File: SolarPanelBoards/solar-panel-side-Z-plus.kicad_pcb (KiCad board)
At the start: 2 copper layers, 97 x 97.4 mm, 23 parts, among them J1 Conn_01x06, J3 Conn_01x02, U1 OPT3001DNPT

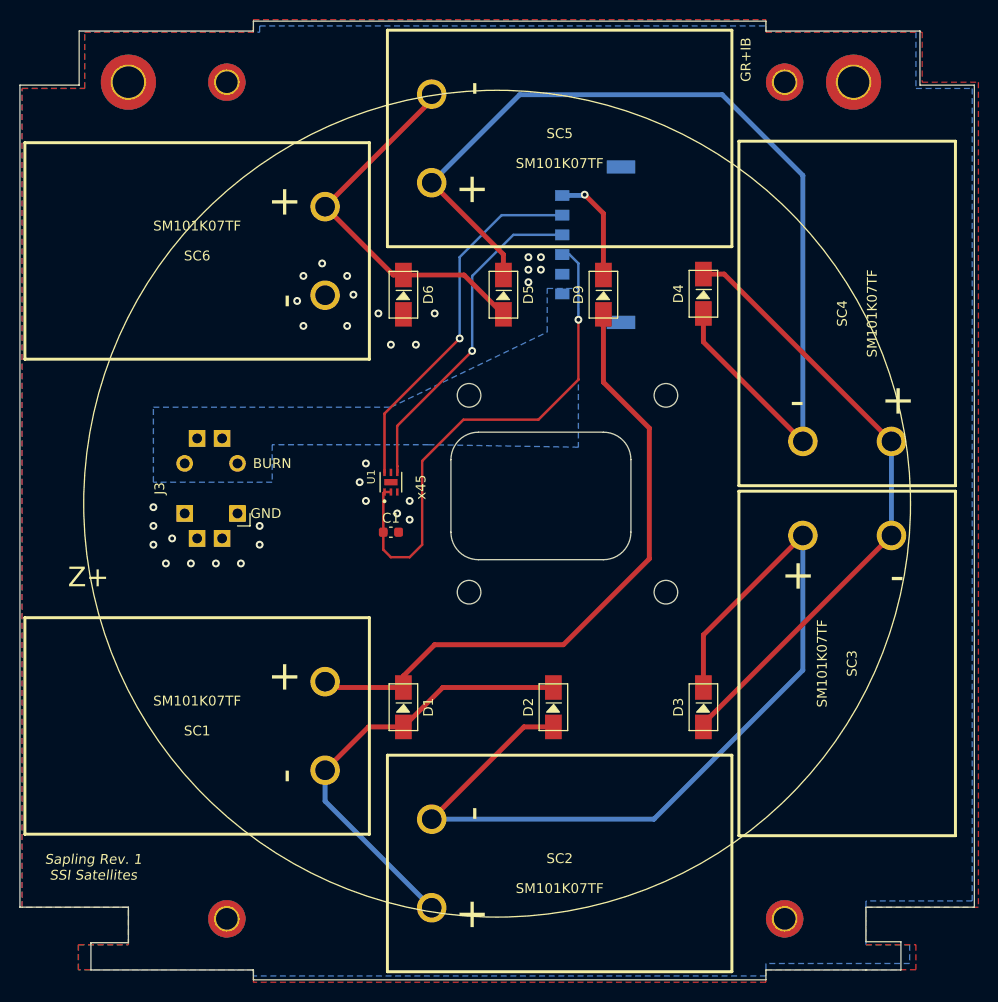
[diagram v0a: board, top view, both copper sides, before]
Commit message: Battery board and side panels ready for CAD check and review, pycubed not finished yet
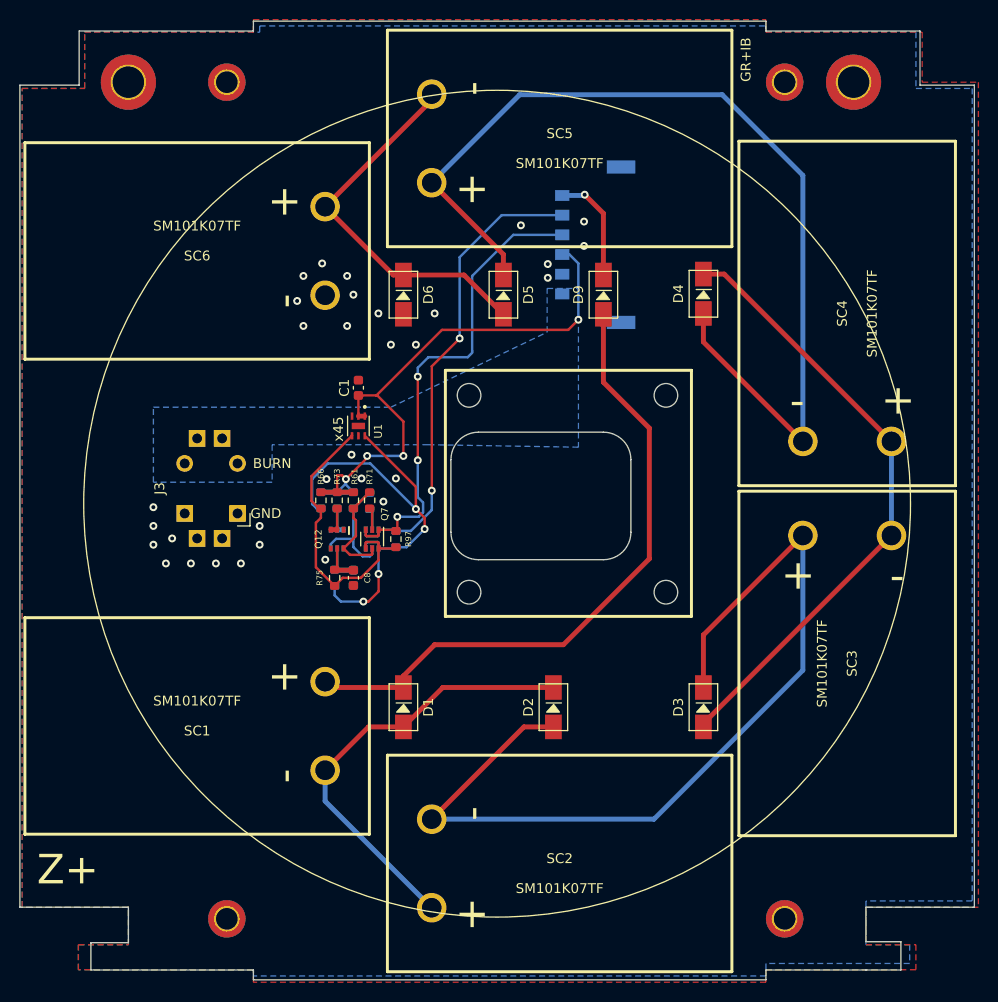
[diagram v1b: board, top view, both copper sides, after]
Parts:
- added C40: 10nF, Capacitor_SMD:C_0603_1608Metric, B.Cu at (134.6, 103.7)
- added C8: 10nF, Capacitor_SMD:C_0603_1608Metric, F.Cu at (134.6, 103.7)
- added Q12: BSS138DWQ-7, sapling:BSS138DWQ-7, F.Cu at (133.0, 99.8)
- added Q13: BSS138DWQ-7, sapling:BSS138DWQ-7, B.Cu at (133.0, 99.8)
- added Q7: MBT2222ADW1T1, Package_TO_SOT_SMD:SOT-363_SC-70-6, F.Cu at (136.5, 99.8)
- added Q8: MBT2222ADW1T1, Package_TO_SOT_SMD:SOT-363_SC-70-6, B.Cu at (136.5, 99.8)
- added R61: 10K, Resistor_SMD:R_0603_1608Metric, F.Cu at (134.6, 95.8)
- added R62: 10K, Resistor_SMD:R_0603_1608Metric, B.Cu at (134.6, 95.8)
- added R66: 10K, Resistor_SMD:R_0603_1608Metric, F.Cu at (131.3, 95.8)
- added R67: 10K, Resistor_SMD:R_0603_1608Metric, B.Cu at (131.3, 95.8)
- added R71: 680, Resistor_SMD:R_0603_1608Metric, F.Cu at (136.3, 95.8)
- added R72: 680, Resistor_SMD:R_0603_1608Metric, B.Cu at (136.3, 95.9)
- added R73: 100K, Resistor_SMD:R_0603_1608Metric, F.Cu at (133.0, 95.8)
- added R74: 100K, Resistor_SMD:R_0603_1608Metric, B.Cu at (133.0, 95.8)
- added R75: 200K, Resistor_SMD:R_0603_1608Metric, F.Cu at (132.7, 103.7)
- added R76: 200K, Resistor_SMD:R_0603_1608Metric, B.Cu at (132.7, 103.7)
- added R97: 0, Resistor_SMD:R_0603_1608Metric, F.Cu at (138.9, 99.8)
- added R98: 0, Resistor_SMD:R_0603_1608Metric, B.Cu at (138.9, 99.8)
- added REF**: CoralCamera, sapling:CoralCamera, F.Cu at (156.5, 81.3)
- moved C1 15.0 mm to (135.1, 84.4), turned to 90 degrees
- moved U1 6.60 mm to (135.1, 88.3), turned to 270 degrees
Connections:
- U1 pad 4: SCL -> SCL_SUN
- U1 pad 6: SDA -> SDA_SUN
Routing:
- net SDA_SUN: track 0.00 -> 47.2 mm, vias 0 -> 4
- net SCL_SUN: track 0.00 -> 29.6 mm
- net SCL: track 34.0 -> 48.4 mm, vias 1 -> 3
- net Net-(Q13-Pad6): track 0.00 -> 12.2 mm
- net Net-(Q12-Pad6): track 0.00 -> 10.8 mm
- net SDA: track 37.2 -> 47.9 mm, vias 1 -> 2
- net +3V3: track 53.0 -> 63.0 mm, vias 1 -> 4
- net Net-(C40-Pad1): track 0.00 -> 4.19 mm
- net Net-(C8-Pad1): track 0.00 -> 4.19 mm
- net Net-(Q13-Pad2): track 0.00 -> 2.81 mm
- net Net-(Q12-Pad2): track 0.00 -> 2.81 mm
- net Net-(Q7-Pad2): track 0.00 -> 2.27 mm
- net Net-(Q8-Pad2): track 0.00 -> 2.20 mm
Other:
- board text added: "+3.3V"
- board text removed: "3.3V"
- board text removed: "Sapling Rev. 1 SSI Satellites"

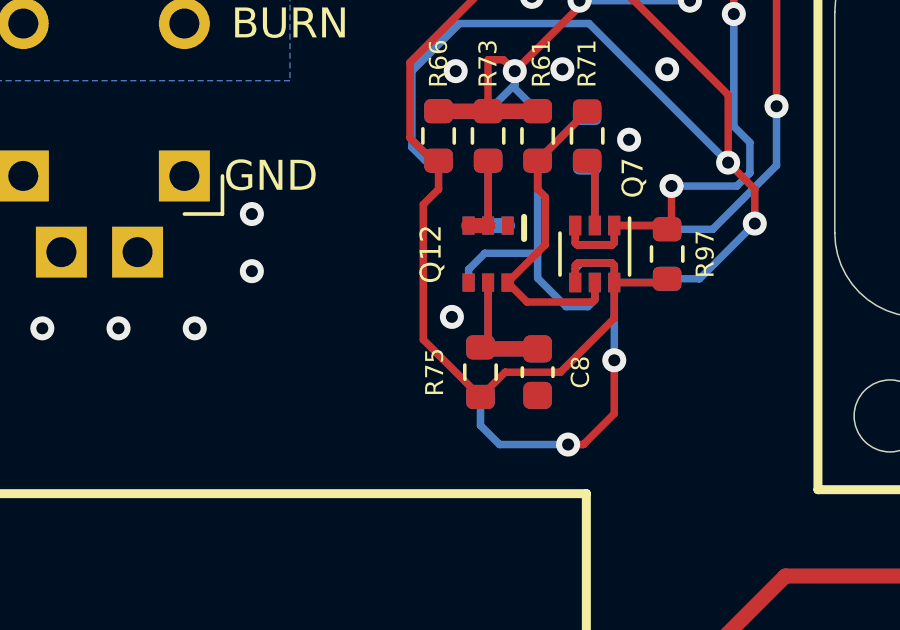
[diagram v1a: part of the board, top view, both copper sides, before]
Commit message: side panels ready except for RF trace width
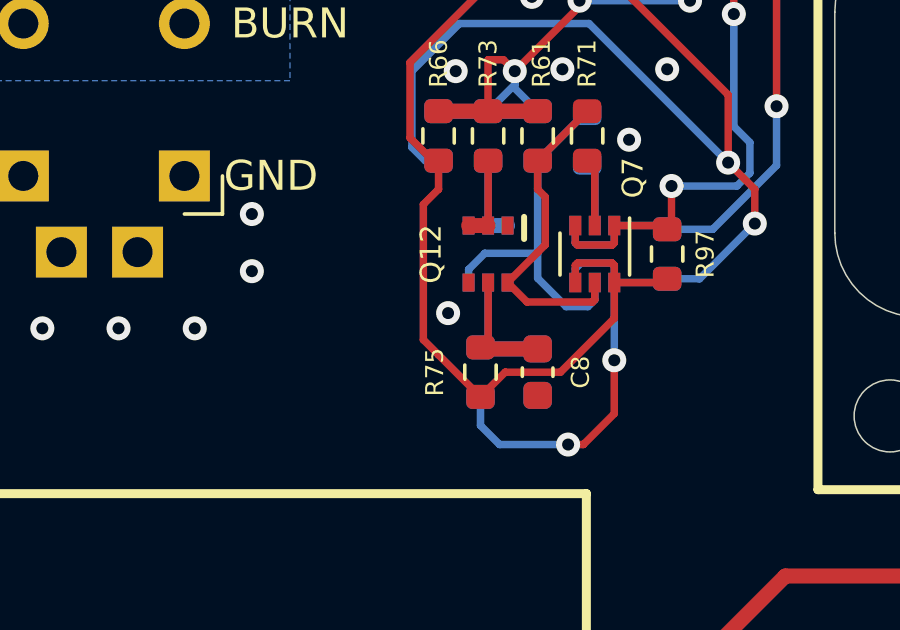
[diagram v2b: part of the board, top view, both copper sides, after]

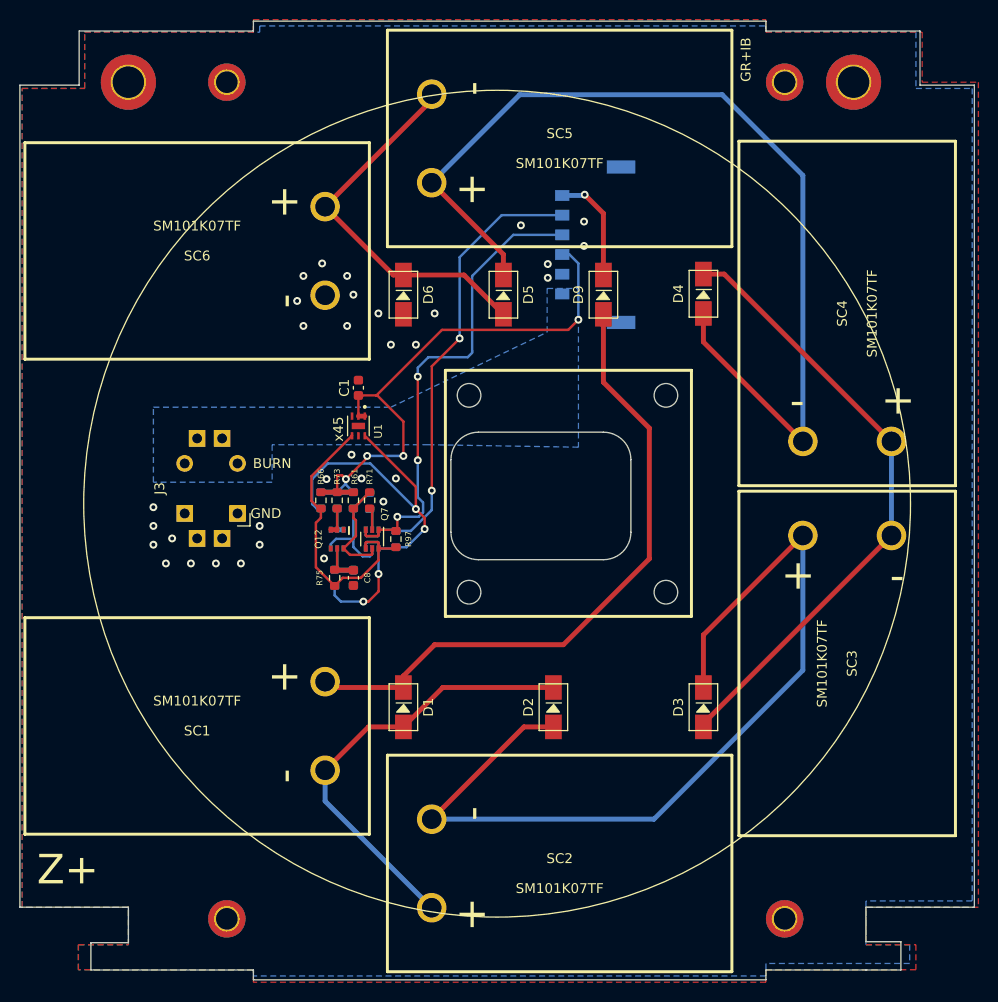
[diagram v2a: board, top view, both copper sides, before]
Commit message: fixed edge cuts of Z+, new step file available
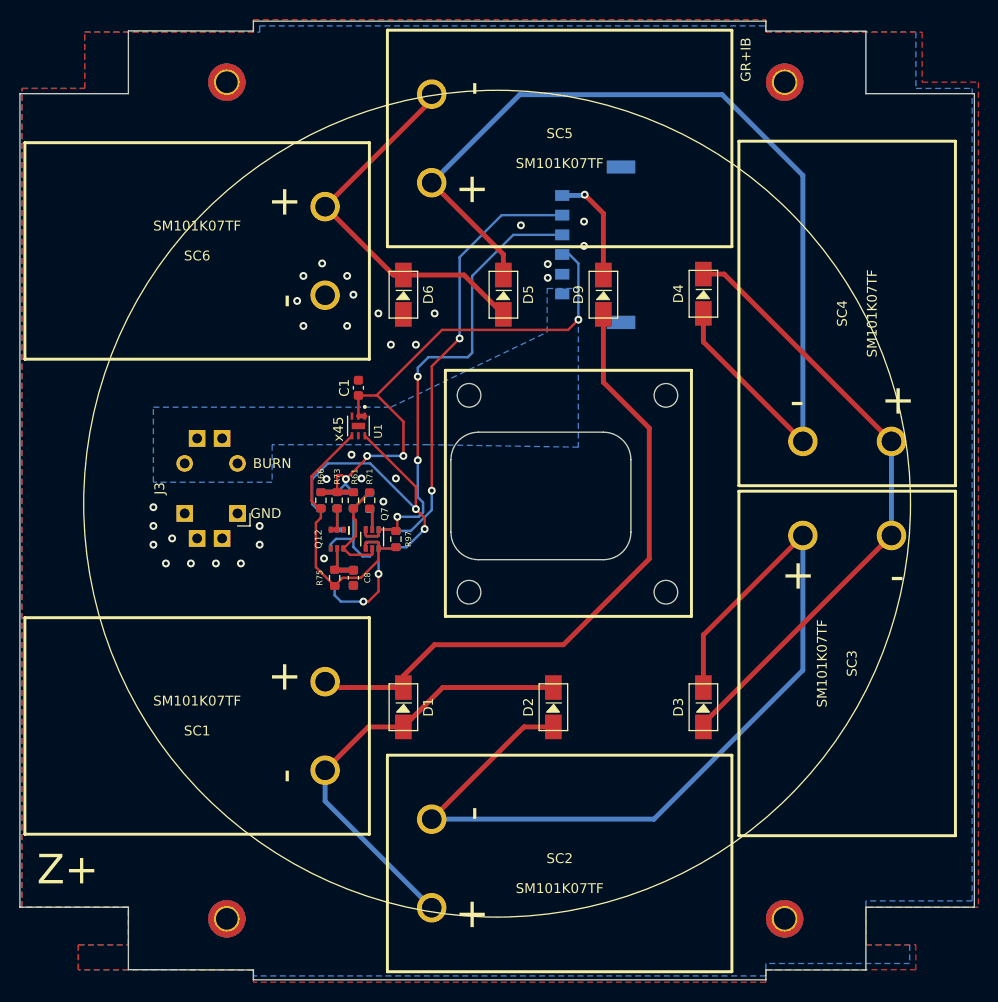
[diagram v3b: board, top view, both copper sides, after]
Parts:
- removed H1, H2: MountingHole_Pad, MountingHole:MountingHole_3.2mm_M3_DIN965_Pad_TopBottom
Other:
- outline, holes or cut-outs redrawn
- board text added: "Grant Regen 2022 Sapling Flight Ver. 1"
